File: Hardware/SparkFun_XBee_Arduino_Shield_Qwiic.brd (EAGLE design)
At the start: 53.3 x 59.7 mm, 181 parts, among them J4 QWIIC_RIGHT_ANGLE, Q1 20V/4.2A/52mΩ/1.4W, Q2 20V/4.2A/52mΩ/1.4W, Q3 3.1A/30V/105mΩ, Q4 5.8A/30V/35mΩ, Q5 20V/4.2A/52mΩ/1.4W, U1 FSUSB30MUX_MSOP10, U2 AP63203, U3 ESD Diode, U4 FT231XS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

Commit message: Adds silk
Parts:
- added U$93: (no value), pot:#IOLED#5
- added U$94: (no value), pot:IO49
- U$52: device topmirror:#PLED#20 -> top:#PLED#20
- moved U$52 0.06 mm to (45.5, 3.00), turned to 0 degrees
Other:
- board text added: "1oz Outer Layer 0.5oz Inner Layer JLC0416H-7628 Stackup"
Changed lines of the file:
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@@
 <text x="6.682" y="39.571" size="1.778" layer="15" font="vector" ratio="15">3</text>
 <text x="8.206" y="39.571" size="1.778" layer="16" font="vector" ratio="15" rot="SMR0">4</text>
-<text x="60.5" y="44.5" size="1.778" layer="51" font="vector" ratio="15">Four Layer Board</text>
-<text x="60.5" y="41" size="1.778" layer="51" font="vector" ratio="15">1.6mm Thickness</text>
-<text x="60.5" y="37.5" size="1.778" layer="51" font="vector" ratio="15">Lead Free HASL</text>
+<text x="59.69" y="44.45" size="1.778" layer="51" font="vector" ratio="15">Four Layer Board</text>
+<text x="59.69" y="26.67" size="1.778" layer="51" font="vector" ratio="15">1.6mm Thickness</text>
+<text x="59.69" y="30.48" size="1.778" layer="51" font="vector" ratio="15">Lead Free HASL</text>
+<text x="59.69" y="34.29" size="1.778" layer="51" font="vector" ratio="15">1oz Outer Layer
+0.5oz Inner Layer
+JLC0416H-7628 Stackup</text>
 </plain>
 <attributes>
@@
 <attribute name="VALUE" x="47.0408" y="12.4968" size="0.6096" layer="27" font="vector" ratio="20" align="top-center"/>
 </element>
-<element name="PLED" library="SparkFun-Jumpers" package="SMT-JUMPER_2_NC_TRACE_SILK" package3d_urn="urn:adsk.eagle:package:39281/1" value="JUMPER-SMT_2_NC_TRACE_SILK" x="42.037" y="3.048" smashed="yes" rot="MR180">
-<attribute name="NAME" x="42.037" y="1.905" size="0.6096" layer="26" font="vector" ratio="20" rot="MR180" align="bottom-center"/>
-<attribute name="VALUE" x="42.037" y="4.191" size="0.6096" layer="28" font="vector" ratio="20" rot="MR180" align="top-center"/>
+<element name="PLED" library="SparkFun-Jumpers" package="SMT-JUMPER_2_NC_TRACE_SILK" package3d_urn="urn:adsk.eagle:package:39281/1" value="JUMPER-SMT_2_NC_TRACE_SILK" x="42.0624" y="3.048" smashed="yes" rot="MR180">
+<attribute name="NAME" x="42.0624" y="1.905" size="0.6096" layer="26" font="vector" ratio="20" rot="MR180" align="bottom-center"/>
+<attribute name="VALUE" x="42.0624" y="4.191" size="0.6096" layer="28" font="vector" ratio="20" rot="MR180" align="top-center"/>
 </element>
 <element name="ALED" library="SparkFun-Jumpers" package="SMT-JUMPER_2_NC_TRACE_SILK" package3d_urn="urn:adsk.eagle:package:39281/1" value="JUMPER-SMT_2_NC_TRACE_SILK" x="50.8" y="15.24" smashed="yes" rot="MR180">
@@
 <element name="U$49" library="topmirror" package="#ALED#21" value="" x="47.244" y="15.24" smashed="yes" rot="MR0"/>
 <element name="U$51" library="topmirror" package="#RLED#22" value="" x="47.244" y="12.7" smashed="yes" rot="MR0"/>
-<element name="U$52" library="topmirror" package="#PLED#20" value="" x="45.466" y="3.0226" smashed="yes" rot="MR180"/>
 <element name="U$21" library="botmirror" package="#TXO#8" value="" x="24.511" y="46.99" smashed="yes"/>
 <element name="U$27" library="botmirror" package="#RXI#7" value="" x="24.1046" y="44.4246" smashed="yes"/>
@@
 <element name="U$91" library="pot" package="D59313" value="" x="48.6918" y="46.9646" smashed="yes"/>
 <element name="U$92" library="pot" package="D9312" value="" x="48.5902" y="44.3738" smashed="yes"/>
+<element name="U$52" library="top" package="#PLED#20" value="" x="45.5168" y="2.9972" smashed="yes" rot="MR0"/>
+<element name="U$93" library="pot" package="#IOLED#5" value="" x="47.117" y="10.16" smashed="yes" rot="MR0"/>
+<element name="U$94" library="pot" package="IO49" value="" x="50.8762" y="11.3538" smashed="yes"/>
 </elements>
 <signals>
@@
 </polygon>
 <wire x1="42.252" y1="6.985" x2="41.4138" y2="6.1468" width="0.254" layer="1"/>
-<wire x1="41.4138" y1="6.1468" x2="41.3766" y2="6.1468" width="0.254" layer="1"/>
 <via x="33.2994" y="14.097" extent="1-16" drill="0.3048"/>
 <via x="36.5506" y="18.0086" extent="1-16" drill="0.3048"/>
@@
 <wire x1="42.557" y1="1.143" x2="43.053" y2="1.143" width="0.254" layer="1"/>
 <via x="43.053" y="1.143" extent="1-16" drill="0.3048"/>
-<wire x1="42.5577" y1="3.048" x2="42.5577" y2="1.6383" width="0.254" layer="16"/>
-<wire x1="42.5577" y1="1.6383" x2="43.053" y2="1.143" width="0.254" layer="16"/>
+<wire x1="42.5831" y1="3.048" x2="42.5831" y2="1.6129" width="0.254" layer="16"/>
+<wire x1="42.5831" y1="1.6129" x2="43.053" y2="1.143" width="0.254" layer="16"/>
 </signal>
 <signal name="N$1">
@@
 </drawing>
 <compatibility>
+<note version="6.3" minversion="6.2.2" severity="warning">
+Since Version 6.2.2 text objects can contain more than one line,
+which will not be processed correctly with this version.
+</note>
 <note version="8.3" severity="warning">
 Since Version 8.3, EAGLE supports URNs for individual library

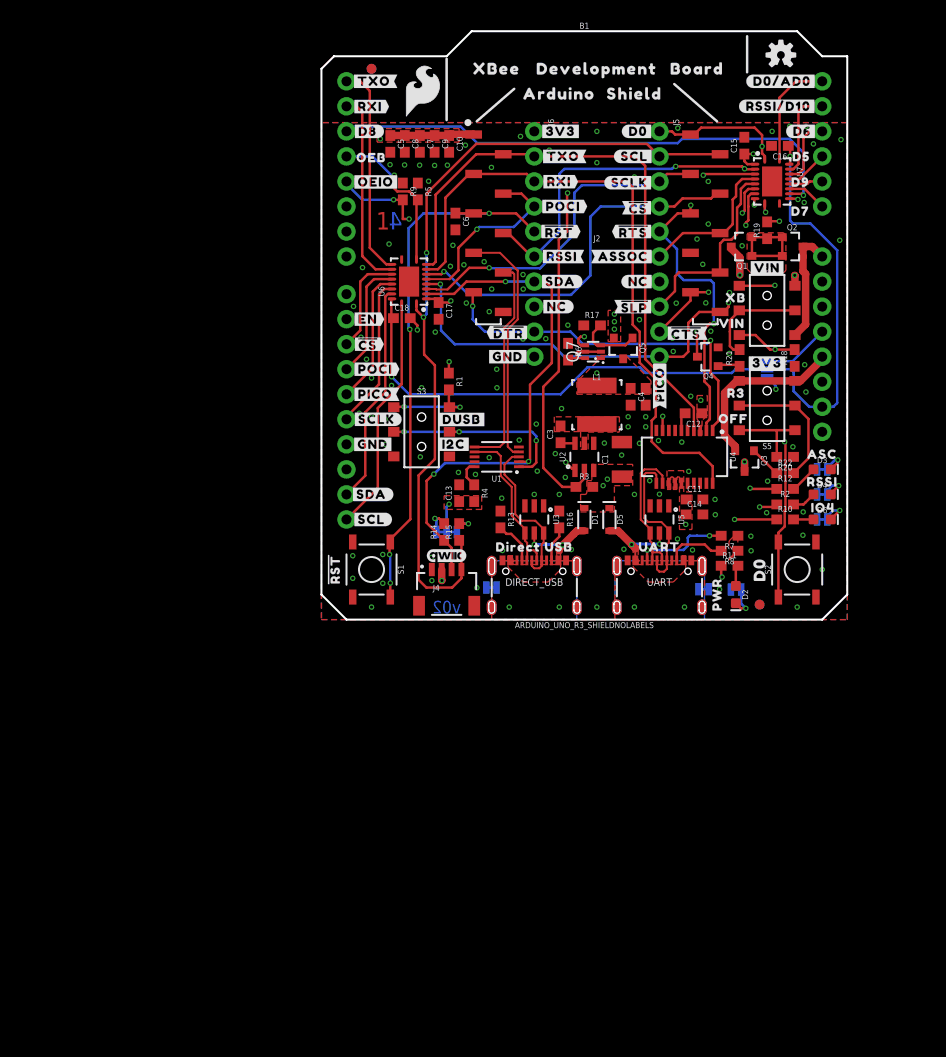
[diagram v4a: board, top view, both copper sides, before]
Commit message: Adds 10k between source and gate on PCHAN circuit
* Switches two resistor values to 0402 so that everything can fit.
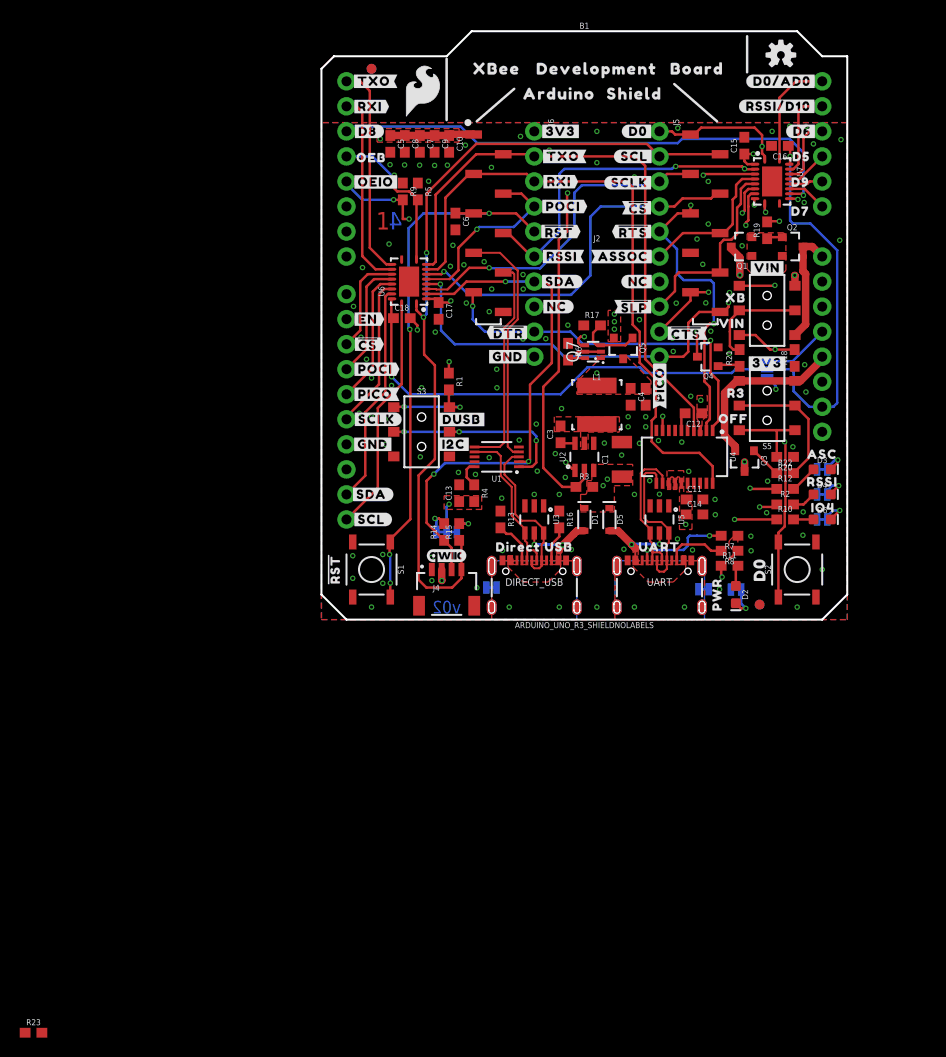
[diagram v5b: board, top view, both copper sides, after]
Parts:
- added R23: 10k, SparkFun-Resistors:0603
- R19: value 10k -> 10
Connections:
- new net N$16: Q1.2, Q2.2, R23.1
- net N$25: now also R23.2; no longer Q1.2, Q2.2
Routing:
- net N$25: track 10.1 -> 1.81 mm
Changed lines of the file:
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@@
 <attribute name="VALUE" x="39.243" y="28.321" size="0.6096" layer="27" font="vector" ratio="20" rot="R180" align="top-center"/>
 </element>
-<element name="R19" library="SparkFun-Resistors" package="0603" value="10k" x="45.212" y="39.497" smashed="yes" rot="R90">
+<element name="R19" library="SparkFun-Resistors" package="0603" value="10" x="45.212" y="39.497" smashed="yes" rot="R90">
 <attribute name="NAME" x="44.45" y="39.497" size="0.6096" layer="25" font="vector" ratio="20" rot="R90" align="bottom-center"/>
-<attribute name="PROD_ID" value="RES-00824" x="45.212" y="39.497" size="1.778" layer="27" font="vector" ratio="15" rot="R90" display="off"/>
-<attribute name="VALUE" x="45.974" y="39.497" size="0.6096" layer="27" font="vector" ratio="20" rot="R90" align="top-center"/>
+<attribute name="PROD_ID" value="RES-09834" x="45.212" y="39.497" size="1.778" layer="27" font="vector" ratio="15" rot="R90" display="off"/>
+<attribute name="VALUE" value="10" x="45.974" y="39.497" size="0.6096" layer="27" font="vector" ratio="20" rot="R90" align="top-center"/>
 </element>
 <element name="R21" library="SparkFun-Resistors" package="0603" value="10k" x="42.418" y="26.543" smashed="yes" rot="R90">
@@
 <element name="U$93" library="pot" package="#IOLED#5" value="" x="47.117" y="10.16" smashed="yes" rot="MR0"/>
 <element name="U$94" library="pot" package="IO49" value="" x="50.8762" y="11.3538" smashed="yes"/>
+<element name="R23" library="SparkFun-Resistors" package="0603" value="10k" x="-29.21" y="-41.91" smashed="yes">
+<attribute name="NAME" x="-29.21" y="-41.148" size="0.6096" layer="25" font="vector" ratio="20" align="bottom-center"/>
+<attribute name="PROD_ID" value="RES-00824" x="-29.21" y="-41.91" size="1.778" layer="27" font="vector" ratio="15" display="off"/>
+<attribute name="VALUE" x="-29.21" y="-42.672" size="0.6096" layer="27" font="vector" ratio="20" align="top-center"/>
+</element>
 </elements>
 <signals>
@@
 </signal>
 <signal name="N$25">
-<contactref element="Q1" pad="2"/>
-<contactref element="Q2" pad="2"/>
 <contactref element="Q2" pad="1"/>
 <contactref element="Q1" pad="1"/>
 <contactref element="R19" pad="1"/>
-<wire x1="46.752" y1="38.796" x2="46.752" y2="36.896" width="0.254" layer="1"/>
-<wire x1="46.752" y1="36.896" x2="43.672" y2="36.896" width="0.254" layer="1"/>
-<wire x1="43.672" y1="36.896" x2="43.672" y2="38.796" width="0.254" layer="1"/>
 <wire x1="46.752" y1="38.796" x2="45.361" y2="38.796" width="0.254" layer="1"/>
 <wire x1="45.361" y1="38.796" x2="45.212" y2="38.647" width="0.254" layer="1"/>
 <wire x1="45.212" y1="38.647" x2="45.063" y2="38.796" width="0.254" layer="1"/>
-<wire x1="45.063" y1="38.796" x2="43.672" y2="38.796" width="0.254" layer="1"/>
 <polygon width="0.254" layer="1" thermals="no">
 <vertex x="47.117" y="35.433"/>
@@
 <vertex x="46.863" y="35.179"/>
 </polygon>
+<contactref element="R23" pad="2"/>
+<wire x1="43.672" y1="36.896" x2="45.212" y2="38.647" width="0" layer="19" extent="1-1"/>
+<wire x1="-28.36" y1="-41.91" x2="43.672" y2="36.896" width="0" layer="19" extent="1-1"/>
 </signal>
 <signal name="N$18">
@@
 <wire x1="47.52" y1="42.7" x2="48.2574" y2="42.7" width="0.254" layer="1"/>
 </signal>
+<signal name="N$16">
+<contactref element="Q1" pad="2"/>
+<contactref element="Q2" pad="2"/>
+<contactref element="R23" pad="1"/>
+<wire x1="46.752" y1="36.896" x2="43.672" y2="38.796" width="0" layer="19" extent="1-1"/>
+<wire x1="-30.06" y1="-41.91" x2="43.672" y2="38.796" width="0" layer="19" extent="1-1"/>
+</signal>
 </signals>

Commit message: Adds more vias
* Improves routing
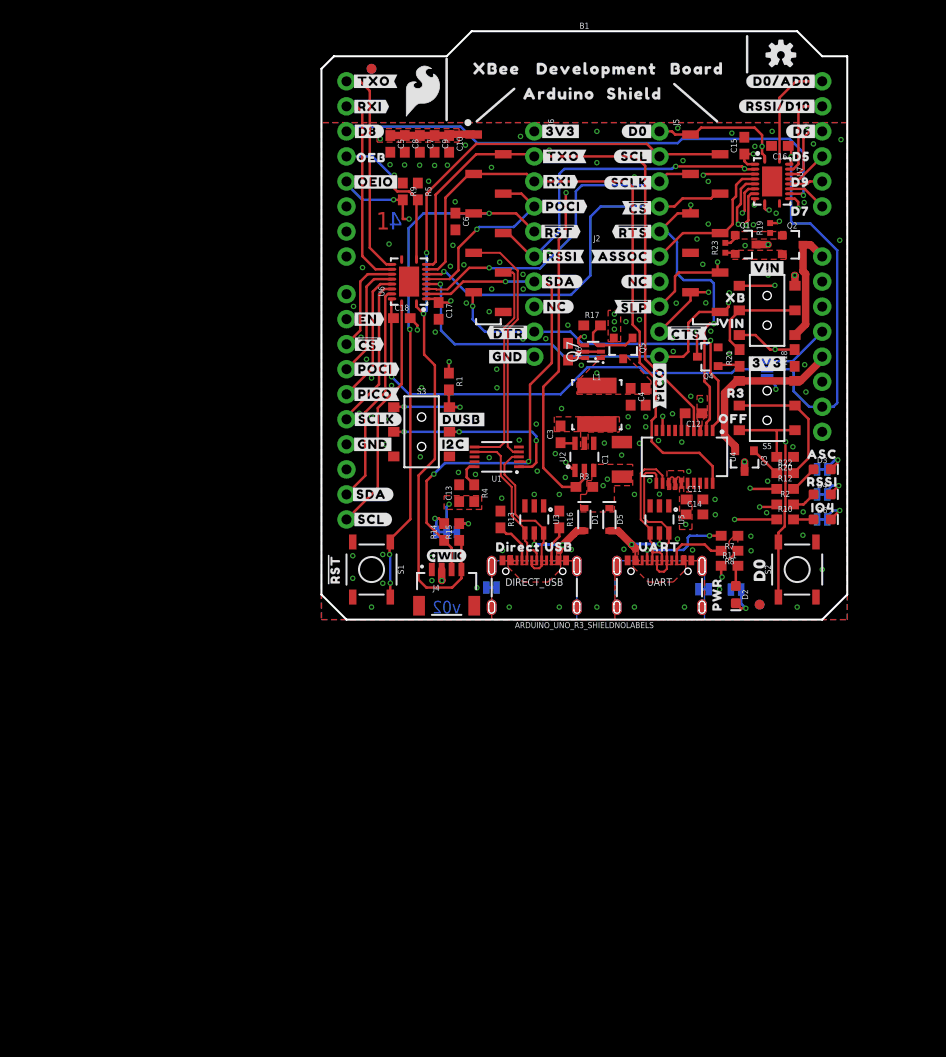
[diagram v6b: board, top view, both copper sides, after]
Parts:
- R19: value 10 -> 10Ω; device SparkFun-Resistors:0603 -> SparkFun-Resistors:0402-TIGHT
- R23: device SparkFun-Resistors:0603 -> SparkFun-Resistors:0402-TIGHT
- moved R23 106.1 mm to (41.0, 37.7), turned to 90 degrees
- moved R19 0.38 mm to (45.5, 39.7)
- moved Q1 0.37 mm to (43.0, 38.0), turned to 270 degrees
- moved Q2 0.18 mm to (47.8, 38.0)
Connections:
- net N$16 renamed SOURCE
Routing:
- net SOURCE: track 0.00 -> 1.06 mm
- net OE_IO: track 46.5 -> 47.1 mm
- net VIN: track 38.5 -> 38.8 mm, vias 4 -> 5
- net D9/!SLEEP!: track 19.8 -> 19.7 mm, vias 0 -> 2
- net GND: vias 116 -> 128
- added copper zone on layer 1, net SOURCE

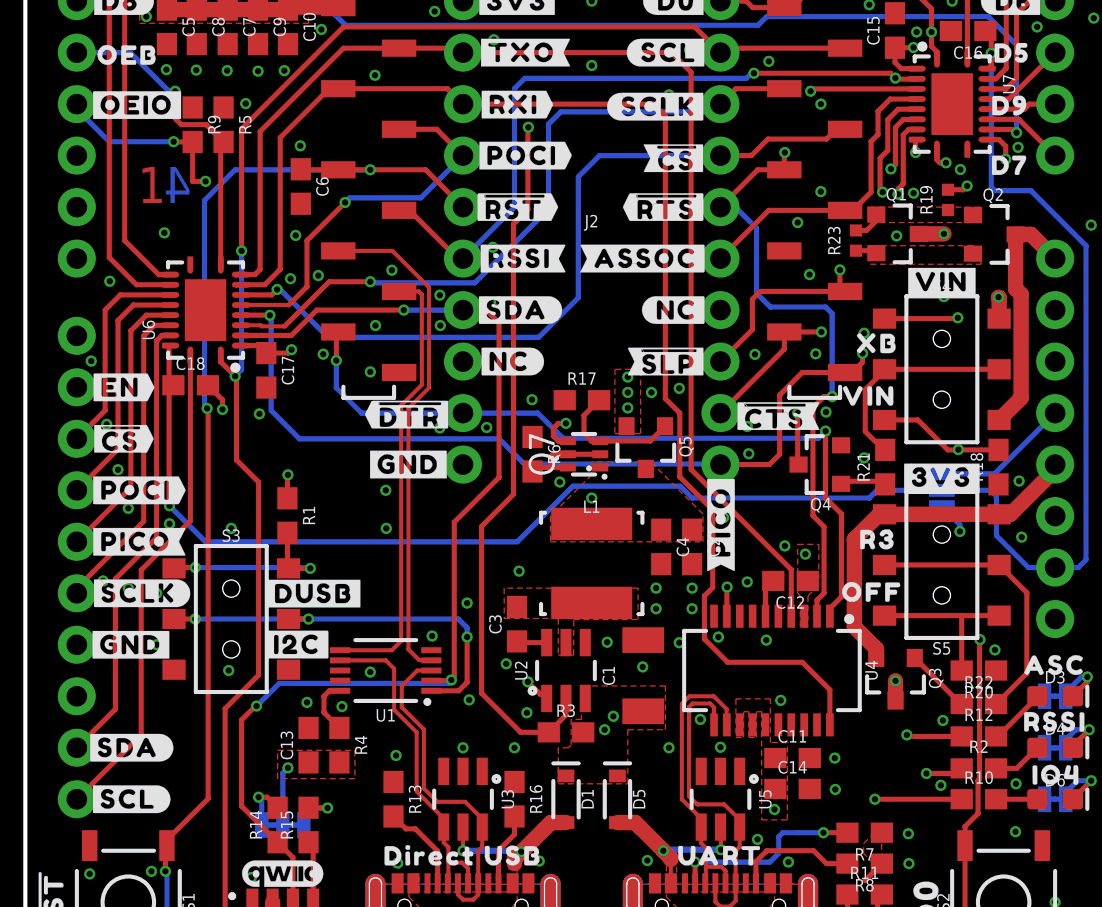
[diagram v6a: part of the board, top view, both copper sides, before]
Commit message: Adds diode to high side switch, adds note to 10k resistor
* Removes voltage divider between NCHAN mosfet and the gates of the PCHAN mosfets
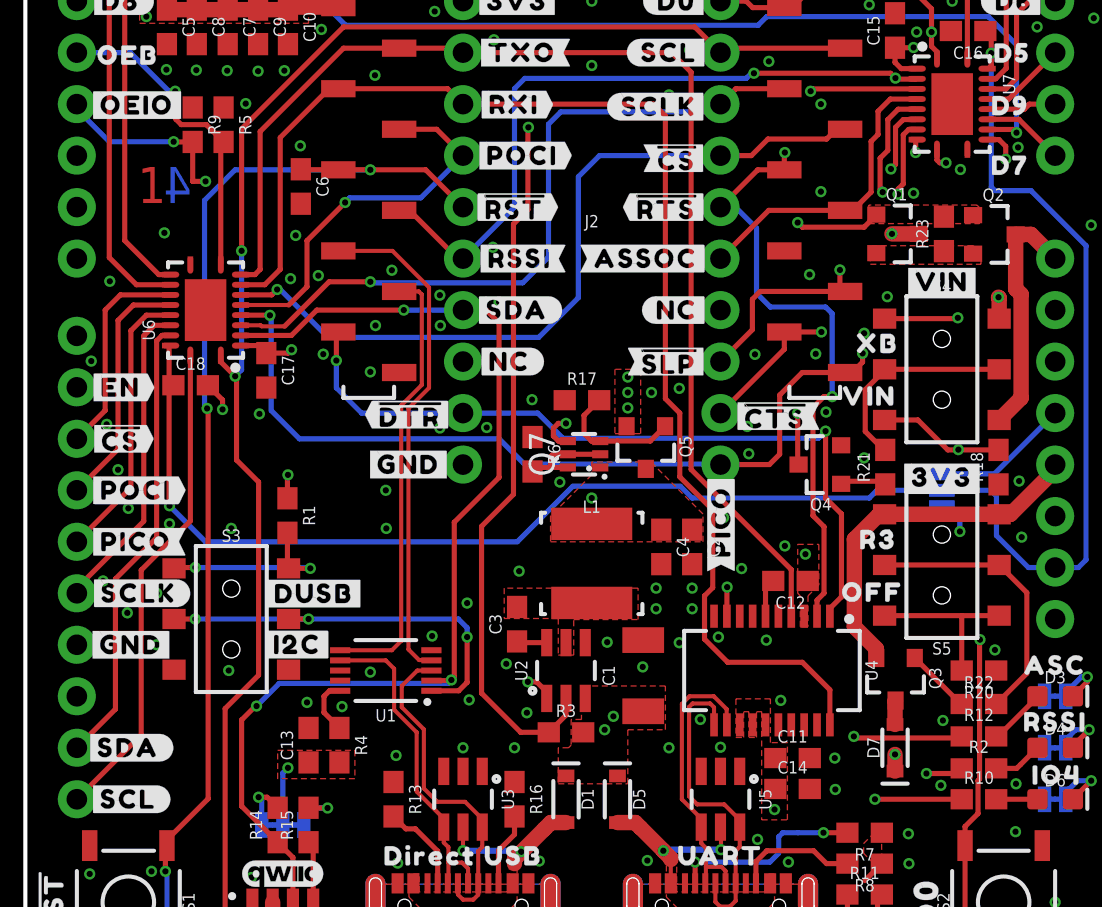
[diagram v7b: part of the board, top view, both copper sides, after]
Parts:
- removed R19: 10Ω, SparkFun-Resistors:0402-TIGHT
- added D7: 3A/10V/280mV, SparkFun-DiscreteSemi:SOD-323
- R23: device SparkFun-Resistors:0402-TIGHT -> SparkFun-Resistors:0603
- moved R23 4.36 mm to (45.3, 38.0)
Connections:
- removed net N$25: Q1.1, Q2.1, R19.1, R23.2
- new net N$16: D7.A, Q3.3
- net 3.3V: now also D7.C; no longer Q3.3
- net N$18: now also Q1.1, Q2.1, R23.2; no longer R19.2
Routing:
- net N$18: track 22.1 -> 16.2 mm, vias 3 -> 2
- net D5/ASSOCIATE: track 51.9 -> 47.8 mm, vias 2 -> 1
- net N$25: track 1.57 -> 0.00 mm
- net D2/SPI_CLK: track 34.1 -> 35.5 mm
- net N$16: track 0.00 -> 1.19 mm
- net SOURCE: track 1.06 -> 0.00 mm
- net VIN: track 38.8 -> 39.7 mm
- added copper zone on layer 1, net N$18
- removed copper zone on layer 1, net N$25
